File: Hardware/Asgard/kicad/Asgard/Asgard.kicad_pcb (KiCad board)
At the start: 2 copper layers, 17.8 x 61 mm, 10 parts

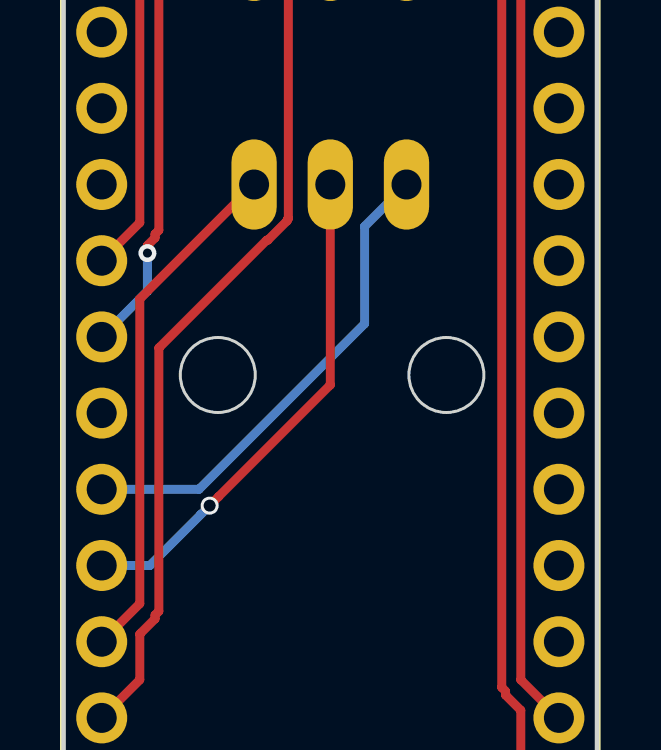
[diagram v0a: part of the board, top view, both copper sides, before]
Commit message: Updated Holes
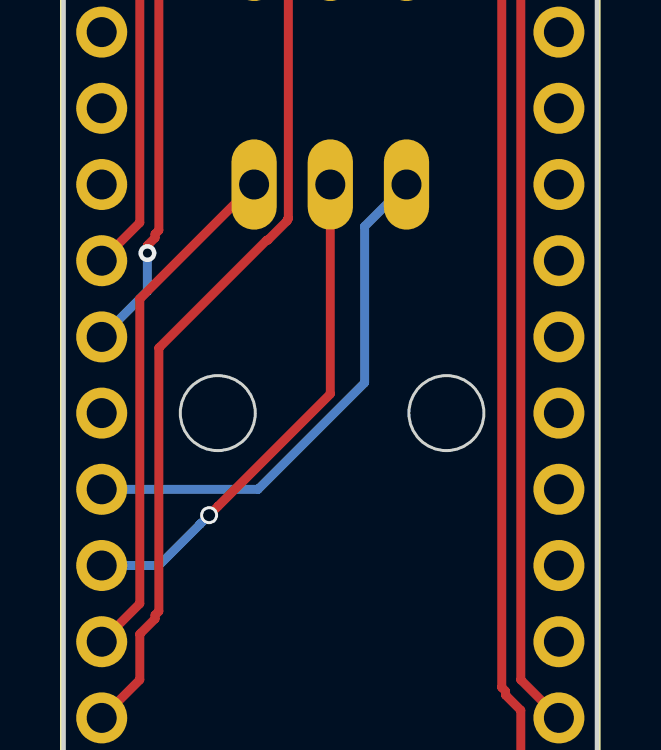
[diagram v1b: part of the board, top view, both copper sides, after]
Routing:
- net Net-(GPIO1-Pad3): track 16.3 -> 17.4 mm
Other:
- outline, holes or cut-outs redrawn
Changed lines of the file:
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@@
   )
   (gr_line (start 40.64 30.48) (end 40.64 91.44) (angle 90) (layer Edge.Cuts) (width 0.15))
-  (gr_circle (center 45.78 73.66) (end 47.03 73.66) (layer Edge.Cuts) (width 0.1))
-  (gr_circle (center 53.4 73.66) (end 54.65 73.66) (layer Edge.Cuts) (width 0.1))
+  (gr_circle (center 45.78 74.93) (end 47.03 74.93) (layer Edge.Cuts) (width 0.1))
+  (gr_circle (center 53.4 74.93) (end 54.65 74.93) (layer Edge.Cuts) (width 0.1))
   (gr_circle (center 52.07 44.45) (end 52.07 46.45) (layer Edge.Cuts) (width 0.1))
   (gr_line (start 58.42 91.44) (end 40.64 91.44) (angle 90) (layer Edge.Cuts) (width 0.15))
@@
   (gr_circle (center 49.53 64.77) (end 49.955 64.77) (layer Dwgs.User) (width 0.1))
   (gr_circle (center 46.99 64.77) (end 47.415 64.77) (layer Dwgs.User) (width 0.1))
-  (gr_circle (center 53.4 73.66) (end 54.65 73.66) (layer Dwgs.User) (width 0.1))
-  (gr_circle (center 45.78 73.66) (end 47.03 73.66) (layer Dwgs.User) (width 0.1))
+  (gr_circle (center 53.4 74.93) (end 54.65 74.93) (layer Dwgs.User) (width 0.1))
+  (gr_circle (center 45.78 74.93) (end 47.03 74.93) (layer Dwgs.User) (width 0.1))
   (gr_line (start 58.32 91.34) (end 40.74 91.34) (layer Dwgs.User) (width 0.1))
   (gr_line (start 40.74 30.58) (end 58.32 30.58) (layer Dwgs.User) (width 0.1))
@@
   (segment (start 43.18 71.12) (end 43.18 81.28) (width 0.3) (layer F.Cu) (net 10) (status 80000))
   (segment (start 43.18 81.28) (end 41.91 82.55) (width 0.3) (layer F.Cu) (net 10) (status 80000))
-  (segment (start 41.91 80.01) (end 43.511878 80.01) (width 0.3) (layer B.Cu) (net 11))
-  (segment (start 45.808049 77.713829) (end 45.50805 78.013828) (width 0.3) (layer F.Cu) (net 11))
-  (segment (start 49.53 73.991878) (end 45.808049 77.713829) (width 0.3) (layer F.Cu) (net 11))
-  (segment (start 49.53 67.31) (end 49.53 73.991878) (width 0.3) (layer F.Cu) (net 11))
-  (via (at 45.50805 78.013828) (size 0.6) (drill 0.4) (layers F.Cu B.Cu) (net 11))
-  (segment (start 45.208051 78.313827) (end 45.50805 78.013828) (width 0.3) (layer B.Cu) (net 11))
-  (segment (start 43.511878 80.01) (end 45.208051 78.313827) (width 0.3) (layer B.Cu) (net 11))
-  (segment (start 50.673 71.94901) (end 50.673 68.707) (width 0.3) (layer B.Cu) (net 48))
-  (segment (start 41.91 77.47) (end 45.15201 77.47) (width 0.3) (layer B.Cu) (net 48))
-  (segment (start 45.15201 77.47) (end 50.673 71.94901) (width 0.3) (layer B.Cu) (net 48))
+  (segment (start 45.190496 78.632081) (end 45.490495 78.332082) (width 0.3) (layer B.Cu) (net 11))
+  (segment (start 43.812577 80.01) (end 45.190496 78.632081) (width 0.3) (layer B.Cu) (net 11))
+  (segment (start 41.91 80.01) (end 43.812577 80.01) (width 0.3) (layer B.Cu) (net 11))
+  (segment (start 45.790494 78.032083) (end 45.490495 78.332082) (width 0.3) (layer F.Cu) (net 11))
+  (segment (start 49.53 74.292577) (end 45.790494 78.032083) (width 0.3) (layer F.Cu) (net 11))
+  (segment (start 49.53 67.31) (end 49.53 74.292577) (width 0.3) (layer F.Cu) (net 11))
+  (via (at 45.490495 78.332082) (size 0.6) (drill 0.4) (layers F.Cu B.Cu) (net 11))
+  (segment (start 47.122043 77.47) (end 50.673 73.919043) (width 0.3) (layer B.Cu) (net 48))
   (segment (start 50.673 68.707) (end 52.07 67.31) (width 0.3) (layer B.Cu) (net 48))
+  (segment (start 41.91 77.47) (end 47.122043 77.47) (width 0.3) (layer B.Cu) (net 48))
+  (segment (start 50.673 73.919043) (end 50.673 68.707) (width 0.3) (layer B.Cu) (net 48))
   (zone (net 6) (net_name GND) (layer B.Cu) (hatch edge 0.508)
     (connect_pads (clearance 0.508))

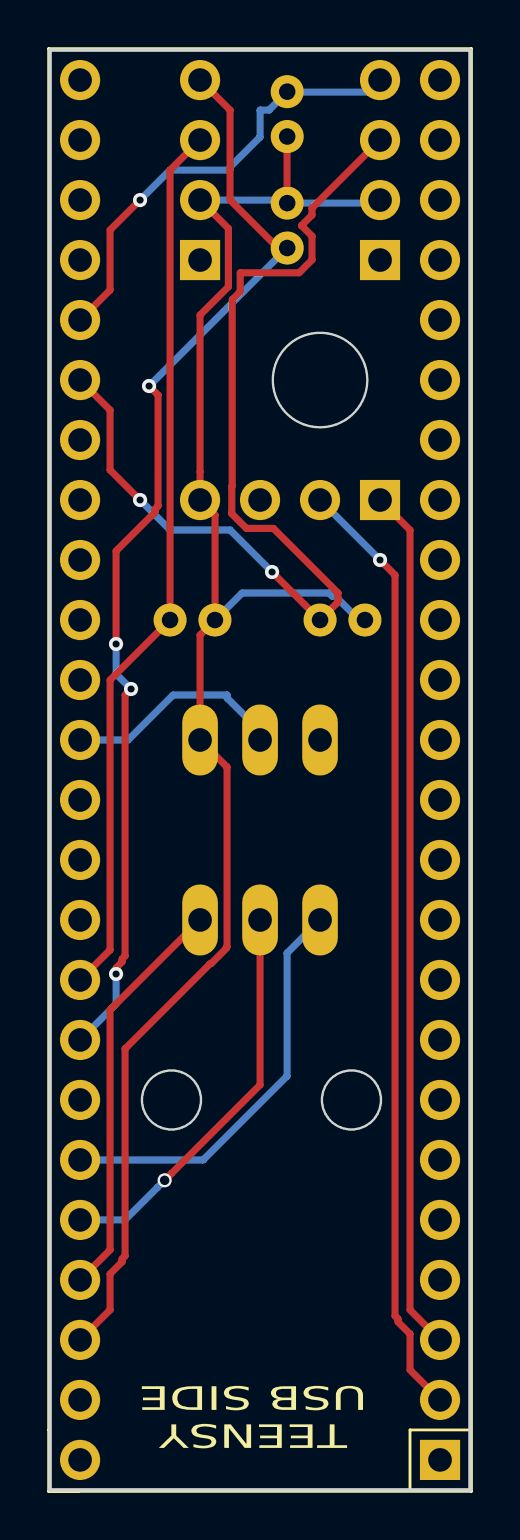
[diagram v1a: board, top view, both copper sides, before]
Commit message: Moved holes in PCB
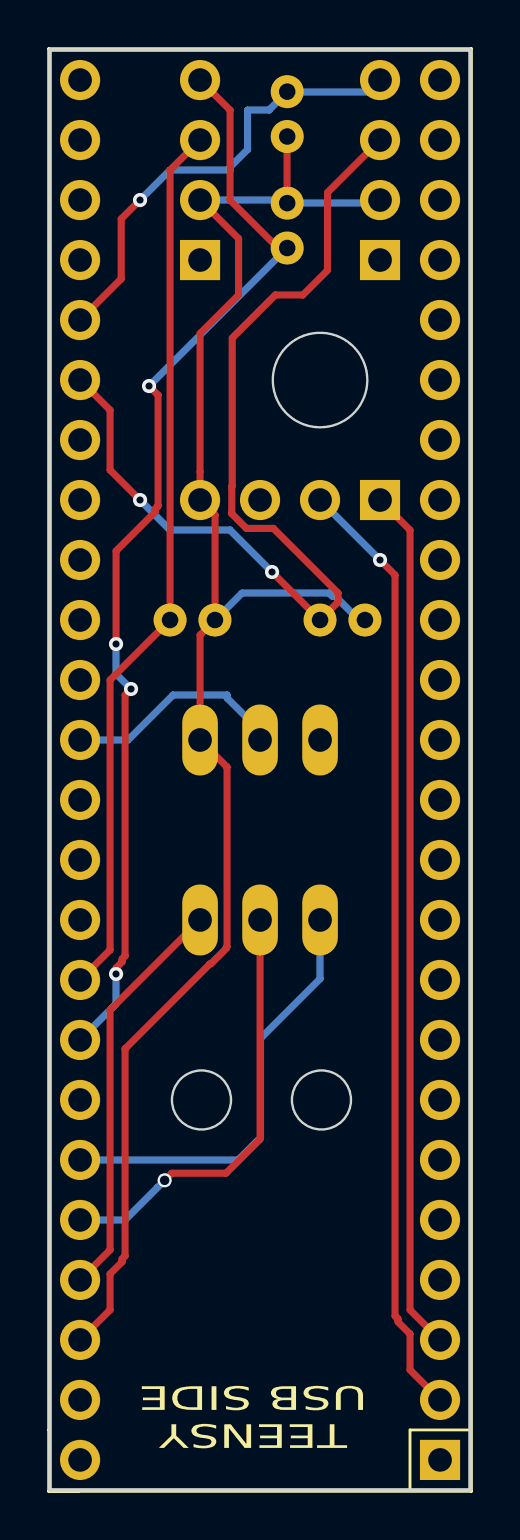
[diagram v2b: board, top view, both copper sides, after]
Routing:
- net Net-(GPIO1-Pad2): track 17.0 -> 18.3 mm
- net Net-(ABSP1-Pad3): track 43.5 -> 42.3 mm
- net Net-(GPIO1-Pad3): track 17.4 -> 18.3 mm
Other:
- outline, holes or cut-outs redrawn

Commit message: Pressure sensors inverted
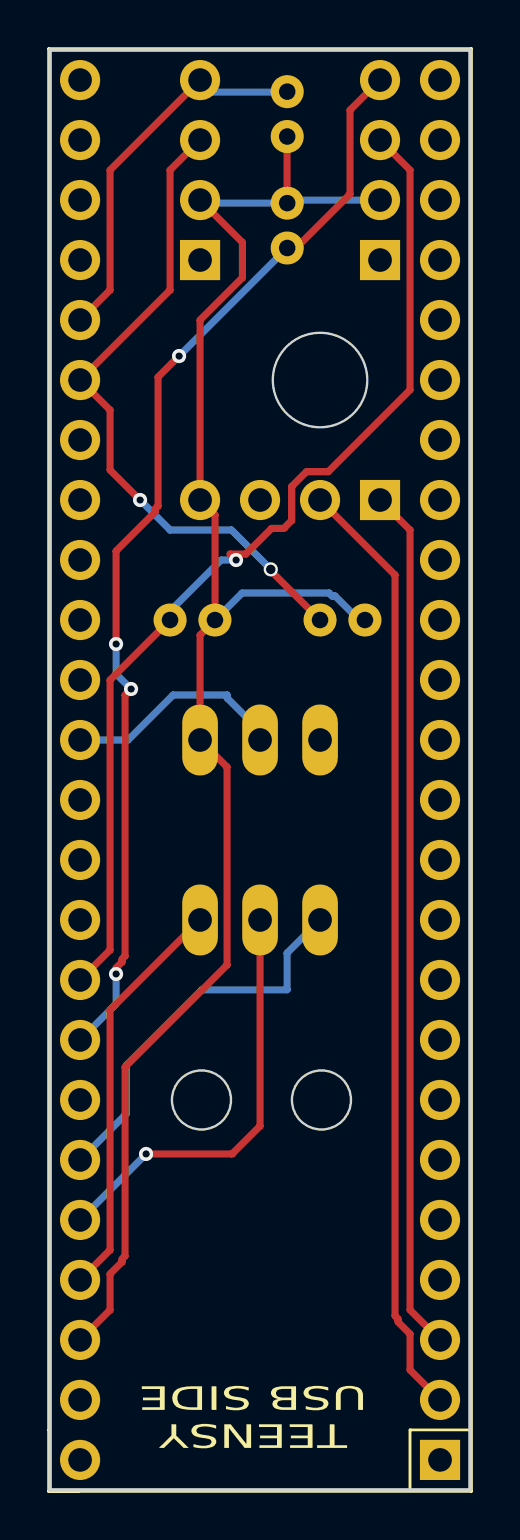
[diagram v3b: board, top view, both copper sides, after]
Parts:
- moved ABSP1 7.62 mm to (47.0, 39.4)
- moved DELTAP1 7.62 mm to (54.6, 39.4)
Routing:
- net Net-(ABSP1-Pad3): track 42.3 -> 28.2 mm
- net Net-(DELTAP1-Pad3): track 37.7 -> 43.7 mm, vias 0 -> 1
- net Net-(ABSP1-Pad4): track 19.5 -> 16.2 mm, vias 1 -> 0
- net Net-(GPIO1-Pad3): track 18.3 -> 16.5 mm
- net Net-(BLUETOOTH1-Pad2): vias 1 -> 0
